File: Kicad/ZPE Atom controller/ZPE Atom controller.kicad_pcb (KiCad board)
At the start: 2 copper layers, 8 parts, among them P1 CONN_01X19, P2 CONN_01X19, Q1 PN2222A, T1 Transformer_SP_1S, U2 LM7805_TO220

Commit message: Updated board
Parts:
- added U1: SSD1306, Package_TO_SOT_SMD:SOT-23-5, F.Cu at (135.1, 99.6)
- P1, P2: value CONN_01X19 -> CONN_01X18
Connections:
- net /SENSOR_VN renamed /IO39
- net /SENSOR_VP renamed /IO36
- P1 pad 1: +3V3 -> (no net)
- P2 pad 1: GND -> (no net)
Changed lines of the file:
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@@
-(kicad_pcb (version 20221232) (generator pcbnew)
+(kicad_pcb (version 20211232) (generator pcbnew)
   (general
     (thickness 1.6)
@@
   (net 10 "+3V3")
   (net 11 "/EN")
-  (net 12 "/SENSOR_VP")
-  (net 13 "/SENSOR_VN")
+  (net 12 "/IO36")
+  (net 13 "/IO39")
   (net 14 "/IO34")
   (net 15 "/IO35")
@@
   (net 43 "/CLK")
   (net 44 "Net-(T1-S1)")
+  (net 45 "unconnected-(U1-NC)")
   (footprint "Connector_PinHeader_2.54mm:PinHeader_1x19_P2.54mm_Vertical" (layer "F.Cu")
     (at 155.37 72.39)
@@
       (effects (font (size 1 1) (thickness 0.15)))
     )
-    (fp_text value "CONN_01X19" (at 0 48.05) (layer "F.Fab")
+    (fp_text value "CONN_01X18" (at 0 48.05) (layer "F.Fab")
       (effects (font (size 1 1) (thickness 0.15)))
     )
@@
     (fp_line (start 1.27 46.99) (end -1.27 46.99)
       (stroke (width 0.1) (type solid)) (layer "F.Fab"))
-    (pad "1" thru_hole rect (at 0 0) (size 1.7 1.7) (drill 1) (layers *.Cu *.Mask)
-      (net 6 "GND") (pinfunction "P1") (pintype "passive"))
+    (pad "1" thru_hole rect (at 0 0) (size 1.7 1.7) (drill 1) (layers *.Cu *.Mask))
     (pad "2" thru_hole oval (at 0 2.54) (size 1.7 1.7) (drill 1) (layers *.Cu *.Mask)
       (net 27 "/IO23") (pinfunction "P2") (pintype "passive"))
@@
     )
   )
+  (footprint "Package_TO_SOT_SMD:SOT-23-5" (layer "F.Cu")
+    (at 135.128 99.568)
+    (descr "SOT, 5 Pin (https://www.jedec.org/sites/default/files/docs/Mo-178c.PDF variant AA), generated with kicad-footprint-generator ipc_gullwing_generator.py")
+    (tags "SOT TO_SOT_SMD")
+    (property "Sheetfile" "ZPE Atom controller.kicad_sch")
+    (property "Sheetname" "")
+    (attr smd)
+    (fp_text reference "U1" (at 0 -2.4) (layer "F.SilkS")
+      (effects (font (size 1 1) (thickness 0.15)))
+    )
+    (fp_text value "SSD1306" (at 0 2.4) (layer "F.Fab")
+      (effects (font (size 1 1) (thickness 0.15)))
+    )
+    (fp_text user "${REFERENCE}" (at 0 0) (layer "F.Fab")
+      (effects (font (size 0.4 0.4) (thickness 0.06)))
+    )
+    (fp_line (start 0 -1.56) (end -1.8 -1.56)
+      (stroke (width 0.12) (type solid)) (layer "F.SilkS"))
+    (fp_line (start 0 -1.56) (end 0.8 -1.56)
+      (stroke (width 0.12) (type solid)) (layer "F.SilkS"))
+    (fp_line (start 0 1.56) (end -0.8 1.56)
+      (stroke (width 0.12) (type solid)) (layer "F.SilkS"))
+    (fp_line (start 0 1.56) (end 0.8 1.56)
+      (stroke (width 0.12) (type solid)) (layer "F.SilkS"))
+    (fp_line (start -2.05 -1.7) (end -2.05 1.7)
+      (stroke (width 0.05) (type solid)) (layer "F.CrtYd"))
+    (fp_line (start -2.05 1.7) (end 2.05 1.7)
+      (stroke (width 0.05) (type solid)) (layer "F.CrtYd"))
+    (fp_line (start 2.05 -1.7) (end -2.05 -1.7)
+      (stroke (width 0.05) (type solid)) (layer "F.CrtYd"))
+    (fp_line (start 2.05 1.7) (end 2.05 -1.7)
+      (stroke (width 0.05) (type solid)) (layer "F.CrtYd"))
+    (fp_line (start -0.8 -1.05) (end -0.4 -1.45)
+      (stroke (width 0.1) (type solid)) (layer "F.Fab"))
+    (fp_line (start -0.8 1.45) (end -0.8 -1.05)
+      (stroke (width 0.1) (type solid)) (layer "F.Fab"))
+    (fp_line (start -0.4 -1.45) (end 0.8 -1.45)
+      (stroke (width 0.1) (type solid)) (layer "F.Fab"))
+    (fp_line (start 0.8 -1.45) (end 0.8 1.45)
+      (stroke (width 0.1) (type solid)) (layer "F.Fab"))
+    (fp_line (start 0.8 1.45) (end -0.8 1.45)
+      (stroke (width 0.1) (type solid)) (layer "F.Fab"))
+    (pad "1" smd roundrect (at -1.1375 -0.95) (size 1.325 0.6) (layers "F.Cu" "F.Paste" "F.Mask") (roundrect_rratio 0.25)
+      (net 6 "GND") (pinfunction "GND") (pintype "power_in"))
+    (pad "2" smd roundrect (at -1.1375 0) (size 1.325 0.6) (layers "F.Cu" "F.Paste" "F.Mask") (roundrect_rratio 0.25)
+      (net 10 "+3V3") (pinfunction "VCC") (pintype "power_in"))
+    (pad "3" smd roundrect (at -1.1375 0.95) (size 1.325 0.6) (layers "F.Cu" "F.Paste" "F.Mask") (roundrect_rratio 0.25)
+      (net 31 "/IO21") (pinfunction "SCL") (pintype "input"))
+    (pad "4" smd roundrect (at 1.1375 0.95) (size 1.325 0.6) (layers "F.Cu" "F.Paste" "F.Mask") (roundrect_rratio 0.25)
+      (net 28 "/IO22") (pinfunction "SDA") (pintype "bidirectional"))
+    (pad "5" smd roundrect (at 1.1375 -0.95) (size 1.325 0.6) (layers "F.Cu" "F.Paste" "F.Mask") (roundrect_rratio 0.25)
+      (net 45 "unconnected-(U1-NC)") (pinfunction "NC") (pintype "no_connect"))
+    (model "${KICAD6_3DMODEL_DIR}/Package_TO_SOT_SMD.3dshapes/SOT-23-5.wrl"
+      (offset (xyz 0 0 0))
+      (scale (xyz 1 1 1))
+      (rotate (xyz 0 0 0))
+    )
+  )
   (footprint "Connector_PinHeader_2.54mm:PinHeader_1x19_P2.54mm_Vertical" (layer "F.Cu")
     (at 160.02 72.39)
@@
       (effects (font (size 1 1) (thickness 0.15)))
     )
-    (fp_text value "CONN_01X19" (at 0 48.05) (layer "F.Fab")
+    (fp_text value "CONN_01X18" (at 0 48.05) (layer "F.Fab")
       (effects (font (size 1 1) (thickness 0.15)))
     )
@@
     (fp_line (start 1.27 46.99) (end -1.27 46.99)
       (stroke (width 0.1) (type solid)) (layer "F.Fab"))
-    (pad "1" thru_hole rect (at 0 0) (size 1.7 1.7) (drill 1) (layers *.Cu *.Mask)
-      (net 10 "+3V3") (pinfunction "P1") (pintype "passive"))
+    (pad "1" thru_hole rect (at 0 0) (size 1.7 1.7) (drill 1) (layers *.Cu *.Mask))
     (pad "2" thru_hole oval (at 0 2.54) (size 1.7 1.7) (drill 1) (layers *.Cu *.Mask)
       (net 11 "/EN") (pinfunction "P2") (pintype "passive"))
     (pad "3" thru_hole oval (at 0 5.08) (size 1.7 1.7) (drill 1) (layers *.Cu *.Mask)
-      (net 12 "/SENSOR_VP") (pinfunction "P3") (pintype "passive"))
+      (net 12 "/IO36") (pinfunction "P3") (pintype "passive"))
     (pad "4" thru_hole oval (at 0 7.62) (size 1.7 1.7) (drill 1) (layers *.Cu *.Mask)
-      (net 13 "/SENSOR_VN") (pinfunction "P4") (pintype "passive"))
+      (net 13 "/IO39") (pinfunction "P4") (pintype "passive"))
     (pad "5" thru_hole oval (at 0 10.16) (size 1.7 1.7) (drill 1) (layers *.Cu *.Mask)
       (net 14 "/IO34") (pinfunction "P5") (pintype "passive"))

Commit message: Updated board
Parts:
- added DutyCycle1: 10k, Potentiometer_THT:Potentiometer_Piher_PC-16_Single_Vertical, F.Cu at (106.1, 104.1)
- added Freq_fine1: 10K, Potentiometer_THT:Potentiometer_Piher_PC-16_Single_Vertical, F.Cu at (84.9, 121.6)
- added Freq_rough1: 10K, Potentiometer_THT:Potentiometer_Piher_PC-16_Single_Vertical, F.Cu at (84.9, 104.1)
- added Freq_super_fine1: 10k, Potentiometer_THT:Potentiometer_Piher_PC-16_Single_Vertical, F.Cu at (127.4, 104.1)
- added Resolution1: 10K, Potentiometer_THT:Potentiometer_Piher_PC-16_Single_Vertical, F.Cu at (106.1, 121.6)
- moved T1 28.4 mm to (205.7, 81.4)
- moved U1 28.1 mm to (142.9, 72.5)
- moved P1 2.84 mm to (162.6, 71.1)
- moved P2 1.33 mm to (154.9, 71.1)

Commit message: Updated schematic
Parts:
- added IC1: TC4424AVPA, Package_DIP:DIP-8_W10.16mm, F.Cu at (94.0, 72.4)
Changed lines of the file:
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@@
   (net 44 "Net-(T1-S1)")
   (net 45 "unconnected-(U1-NC)")
+  (net 46 "unconnected-(IC1-NC_2)")
+  (net 47 "unconnected-(IC1-IN_B)")
+  (net 48 "unconnected-(IC1-OUT_B)")
+  (net 49 "Net-(Q2-G)")
+  (net 50 "unconnected-(IC1-NC)")
   (footprint "Connector_PinHeader_2.54mm:PinHeader_1x19_P2.54mm_Vertical" (layer "F.Cu")
     (at 154.94 71.13)
@@
       (offset (xyz 0 0 0))
       (scale (xyz 1 1 1))
+      (rotate (xyz 0 0 0))
+    )
+  )
+  (footprint "Package_DIP:DIP-8_W10.16mm" (layer "F.Cu")
+    (at 93.96 72.4)
+    (descr "8-lead though-hole mounted DIP package, row spacing 10.16 mm (400 mils)")
+    (tags "THT DIP DIL PDIP 2.54mm 10.16mm 400mil")
+    (property "Arrow Part Number" "TC4424AVPA")
+    (property "Arrow Price/Stock" "https://www.arrow.com/en/products/tc4424avpa/microchip-technology?region=nac")
+    (property "Description" "Microchip TC4424AVPA, Dual MOSFET Power Driver 4.5A, 4.5  18 V, Non-Inverting, 8-Pin PDIP")
+    (property "Height" "")
+    (property "Manufacturer_Name" "Microchip")
+    (property "Manufacturer_Part_Number" "TC4424AVPA")
+    (property "Mouser Part Number" "579-TC4424AVPA")
+    (property "Mouser Price/Stock" "https://www.mouser.co.uk/ProductDetail/Microchip-Technology/TC4424AVPA?qs=AkCjCAp%252BzjQ%252BX%2F9zoVOWQw%3D%3D")
+    (property "Sheetfile" "ZPE Atom controller.kicad_sch")
+    (property "Sheetname" "")
+    (attr through_hole)
+    (fp_text reference "IC1" (at 5.08 -2.33) (layer "F.SilkS")
+      (effects (font (size 1 1) (thickness 0.15)))
+    )
+    (fp_text value "TC4424AVPA" (at 5.08 9.95) (layer "F.Fab")
+      (effects (font (size 1 1) (thickness 0.15)))
+    )
+    (fp_text user "${REFERENCE}" (at 5.08 3.81) (layer "F.Fab")
+      (effects (font (size 1 1) (thickness 0.15)))
+    )
+    (fp_line (start 1.845 -1.33) (end 1.845 8.95)
+      (stroke (width 0.12) (type solid)) (layer "F.SilkS"))
+    (fp_line (start 1.845 8.95) (end 8.315 8.95)
+      (stroke (width 0.12) (type solid)) (layer "F.SilkS"))
+    (fp_line (start 4.08 -1.33) (end 1.845 -1.33)
+      (stroke (width 0.12) (type solid)) (layer "F.SilkS"))
+    (fp_line (start 8.315 -1.33) (end 6.08 -1.33)
+      (stroke (width 0.12) (type solid)) (layer "F.SilkS"))
+    (fp_line (start 8.315 8.95) (end 8.315 -1.33)
+      (stroke (width 0.12) (type solid)) (layer "F.SilkS"))
+    (fp_arc (start 6.08 -1.33) (mid 5.08 -0.33) (end 4.08 -1.33)
+      (stroke (width 0.12) (type solid)) (layer "F.SilkS"))
+    (fp_line (start -1.05 -1.55) (end -1.05 9.15)
+      (stroke (width 0.05) (type solid)) (layer "F.CrtYd"))
+    (fp_line (start -1.05 9.15) (end 11.25 9.15)
+      (stroke (width 0.05) (type solid)) (layer "F.CrtYd"))
+    (fp_line (start 11.25 -1.55) (end -1.05 -1.55)
+      (stroke (width 0.05) (type solid)) (layer "F.CrtYd"))
+    (fp_line (start 11.25 9.15) (end 11.25 -1.55)
+      (stroke (width 0.05) (type solid)) (layer "F.CrtYd"))
+    (fp_line (start 1.905 -0.27) (end 2.905 -1.27)
+      (stroke (width 0.1) (type solid)) (layer "F.Fab"))
+    (fp_line (start 1.905 8.89) (end 1.905 -0.27)
+      (stroke (width 0.1) (type solid)) (layer "F.Fab"))
+    (fp_line (start 2.905 -1.27) (end 8.255 -1.27)
+      (stroke (width 0.1) (type solid)) (layer "F.Fab"))
+    (fp_line (start 8.255 -1.27) (end 8.255 8.89)
+      (stroke (width 0.1) (type solid)) (layer "F.Fab"))
+    (fp_line (start 8.255 8.89) (end 1.905 8.89)
+      (stroke (width 0.1) (type solid)) (layer "F.Fab"))
+    (pad "1" thru_hole rect (at 0 0) (size 1.6 1.6) (drill 0.8) (layers *.Cu *.Mask)
+      (net 46 "unconnected-(IC1-NC_2)") (pinfunction "NC_2") (pintype "passive"))
+    (pad "2" thru_hole oval (at 0 2.54) (size 1.6 1.6) (drill 0.8) (layers *.Cu *.Mask)
+      (net 17 "/IO33") (pinfunction "IN_A") (pintype "passive"))
+    (pad "3" thru_hole oval (at 0 5.08) (size 1.6 1.6) (drill 0.8) (layers *.Cu *.Mask)
+      (net 6 "GND") (pinfunction "GND") (pintype "passive"))
+    (pad "4" thru_hole oval (at 0 7.62) (size 1.6 1.6) (drill 0.8) (layers *.Cu *.Mask)
+      (net 47 "unconnected-(IC1-IN_B)") (pinfunction "IN_B") (pintype "passive"))
+    (pad "5" thru_hole oval (at 10.16 7.62) (size 1.6 1.6) (drill 0.8) (layers *.Cu *.Mask)
+      (net 48 "unconnected-(IC1-OUT_B)") (pinfunction "OUT_B") (pintype "passive"))
+    (pad "6" thru_hole oval (at 10.16 5.08) (size 1.6 1.6) (drill 0.8) (layers *.Cu *.Mask)
+      (net 1 "+12V") (pinfunction "VDD") (pintype "passive"))
+    (pad "7" thru_hole oval (at 10.16 2.54) (size 1.6 1.6) (drill 0.8) (layers *.Cu *.Mask)
+      (net 49 "Net-(Q2-G)") (pinfunction "OUT_A") (pintype "passive"))
+    (pad "8" thru_hole oval (at 10.16 0) (size 1.6 1.6) (drill 0.8) (layers *.Cu *.Mask)
+      (net 50 "unconnected-(IC1-NC)") (pinfunction "NC") (pintype "no_connect"))
+    (model "${KICAD6_3DMODEL_DIR}/Package_DIP.3dshapes/DIP-8_W10.16mm.wrl"
+      (offset (xyz 0 0 0))
+      (scale (xyz 1 1 1))

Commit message: updated
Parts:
- added R1: 4.7k, Resistor_THT:R_Axial_DIN0207_L6.3mm_D2.5mm_P10.16mm_Horizontal, F.Cu at (167.6, 99.1)
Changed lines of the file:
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@@
       (dashed_line_dash_ratio 12.000000)
       (dashed_line_gap_ratio 3.000000)
-      (svguseinch false)
       (svgprecision 6)
       (excludeedgelayer true)
@@
   (net 47 "unconnected-(IC1-IN_B)")
   (net 48 "unconnected-(IC1-OUT_B)")
-  (net 49 "Net-(Q2-G)")
+  (net 49 "Net-(IC1-OUT_A)")
   (net 50 "unconnected-(IC1-NC)")
   (footprint "Connector_PinHeader_2.54mm:PinHeader_1x19_P2.54mm_Vertical" (layer "F.Cu")
@@
       (net 1 "+12V") (pinfunction "VDD") (pintype "passive"))
     (pad "7" thru_hole oval (at 10.16 2.54) (size 1.6 1.6) (drill 0.8) (layers *.Cu *.Mask)
-      (net 49 "Net-(Q2-G)") (pinfunction "OUT_A") (pintype "passive"))
+      (net 49 "Net-(IC1-OUT_A)") (pinfunction "OUT_A") (pintype "passive"))
     (pad "8" thru_hole oval (at 10.16 0) (size 1.6 1.6) (drill 0.8) (layers *.Cu *.Mask)
       (net 50 "unconnected-(IC1-NC)") (pinfunction "NC") (pintype "no_connect"))
@@
       (offset (xyz 0 0 0))
       (scale (xyz 1 1 1))
+      (rotate (xyz 0 0 0))
+    )
+  )
+  (footprint "Resistor_THT:R_Axial_DIN0207_L6.3mm_D2.5mm_P10.16mm_Horizontal" (layer "F.Cu")
+    (at 167.64 99.06)
+    (descr "Resistor, Axial_DIN0207 series, Axial, Horizontal, pin pitch=10.16mm, 0.25W = 1/4W, length*diameter=6.3*2.5mm^2, http://cdn-reichelt.de/documents/datenblatt/B400/1_4W%23YAG.pdf")
+    (tags "Resistor Axial_DIN0207 series Axial Horizontal pin pitch 10.16mm 0.25W = 1/4W length 6.3mm diameter 2.5mm")
+    (property "Sheetfile" "ZPE Atom controller.kicad_sch")
+    (property "Sheetname" "")
+    (attr through_hole)
+    (fp_text reference "R1" (at 5.08 -2.37) (layer "F.SilkS")
+      (effects (font (size 1 1) (thickness 0.15)))
+    )
+    (fp_text value "4.7k" (at 5.08 2.37) (layer "F.Fab")
+      (effects (font (size 1 1) (thickness 0.15)))
+    )
+    (fp_text user "${REFERENCE}" (at 5.08 0) (layer "F.Fab")
+      (effects (font (size 1 1) (thickness 0.15)))
+    )
+    (fp_line (start 1.04 0) (end 1.81 0)
+      (stroke (width 0.12) (type solid)) (layer "F.SilkS"))
+    (fp_line (start 1.81 -1.37) (end 1.81 1.37)
+      (stroke (width 0.12) (type solid)) (layer "F.SilkS"))
+    (fp_line (start 1.81 1.37) (end 8.35 1.37)
+      (stroke (width 0.12) (type solid)) (layer "F.SilkS"))
+    (fp_line (start 8.35 -1.37) (end 1.81 -1.37)
+      (stroke (width 0.12) (type solid)) (layer "F.SilkS"))
+    (fp_line (start 8.35 1.37) (end 8.35 -1.37)
+      (stroke (width 0.12) (type solid)) (layer "F.SilkS"))
+    (fp_line (start 9.12 0) (end 8.35 0)
+      (stroke (width 0.12) (type solid)) (layer "F.SilkS"))
+    (fp_line (start -1.05 -1.5) (end -1.05 1.5)
+      (stroke (width 0.05) (type solid)) (layer "F.CrtYd"))
+    (fp_line (start -1.05 1.5) (end 11.21 1.5)
+      (stroke (width 0.05) (type solid)) (layer "F.CrtYd"))
+    (fp_line (start 11.21 -1.5) (end -1.05 -1.5)
+      (stroke (width 0.05) (type solid)) (layer "F.CrtYd"))
+    (fp_line (start 11.21 1.5) (end 11.21 -1.5)
+      (stroke (width 0.05) (type solid)) (layer "F.CrtYd"))
+    (fp_line (start 0 0) (end 1.93 0)
+      (stroke (width 0.1) (type solid)) (layer "F.Fab"))
+    (fp_line (start 1.93 -1.25) (end 1.93 1.25)
+      (stroke (width 0.1) (type solid)) (layer "F.Fab"))
+    (fp_line (start 1.93 1.25) (end 8.23 1.25)
+      (stroke (width 0.1) (type solid)) (layer "F.Fab"))
+    (fp_line (start 8.23 -1.25) (end 1.93 -1.25)
+      (stroke (width 0.1) (type solid)) (layer "F.Fab"))
+    (fp_line (start 8.23 1.25) (end 8.23 -1.25)
+      (stroke (width 0.1) (type solid)) (layer "F.Fab"))
+    (fp_line (start 10.16 0) (end 8.23 0)
+      (stroke (width 0.1) (type solid)) (layer "F.Fab"))
+    (pad "1" thru_hole circle (at 0 0) (size 1.6 1.6) (drill 0.8) (layers *.Cu *.Mask)
+      (net 17 "/IO33") (pintype "passive"))
+    (pad "2" thru_hole oval (at 10.16 0) (size 1.6 1.6) (drill 0.8) (layers *.Cu *.Mask)
+      (net 6 "GND") (pintype "passive"))
+    (model "${KICAD6_3DMODEL_DIR}/Resistor_THT.3dshapes/R_Axial_DIN0207_L6.3mm_D2.5mm_P10.16mm_Horizontal.wrl"
+      (offset (xyz 0 0 0))
+      (scale (xyz 1 1 1))

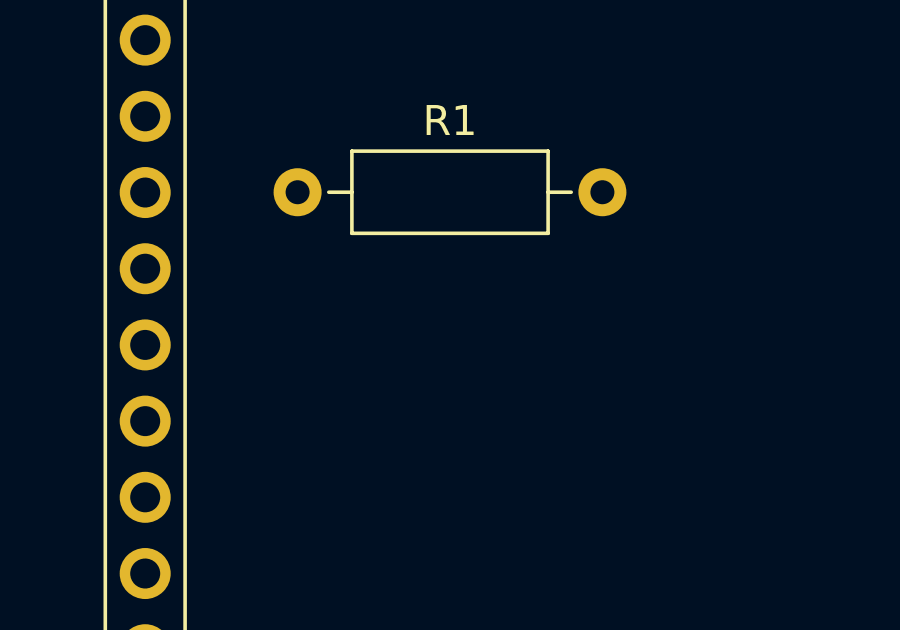
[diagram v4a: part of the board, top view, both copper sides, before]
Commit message: Added resistor before MOSFET
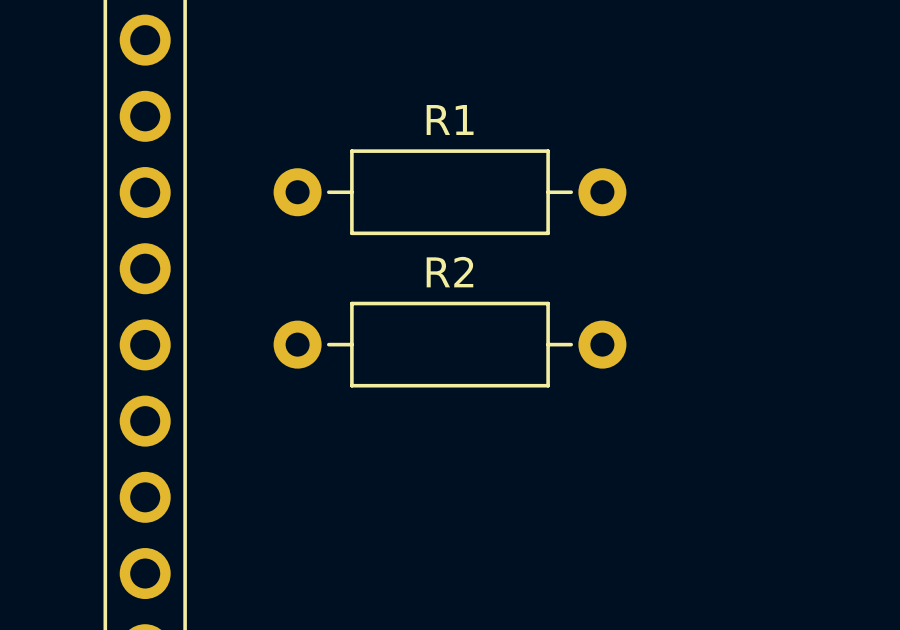
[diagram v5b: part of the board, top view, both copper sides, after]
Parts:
- added R2: 1k, Resistor_THT:R_Axial_DIN0207_L6.3mm_D2.5mm_P10.16mm_Horizontal, F.Cu at (167.6, 104.1)
